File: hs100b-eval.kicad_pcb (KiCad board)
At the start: 2 copper layers, 60 x 50 mm, 42 parts, among them IC1 HS-100B, J1 SPKR, J2 MIC, J3 RADIO_DATA, SW1 MUTE_REC, SW2 MUTE_PLAY, SW3 VOL_DN, SW4 VOL_UP

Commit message: Add more test points
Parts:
- added TP1: GND, TestPoint:TestPoint_Pad_D2.0mm, F.Cu at (148.0, 72.0)
- added TP2: 5V, TestPoint:TestPoint_Pad_D1.0mm, F.Cu at (174.0, 74.0)
- TP3: renamed from TP1; value Test_3V3 -> 3V3
- moved TP3 38.0 mm to (148.5, 80.0)
- moved J1 2.50 mm to (138.0, 111.0)
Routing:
- net +3V3: track 72.6 -> 43.3 mm
- net /AUDIO_R: track 37.9 -> 22.4 mm, vias 2 -> 0
- net VBUS: track 37.8 -> 41.4 mm
- net /AUDIO_L: track 30.2 -> 26.8 mm
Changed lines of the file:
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@@
-(kicad_pcb (version 20171130) (host pcbnew 5.1.9)
+(kicad_pcb (version 20171130) (host pcbnew "(5.1.9-0-10_14)")
   (general
     (thickness 1.6)
     (drawings 8)
-    (tracks 333)
+    (tracks 323)
     (zones 0)
-    (modules 42)
+    (modules 44)
     (nets 37)
   )
@@
     (add_net /USB-)
   )
+  (module TestPoint:TestPoint_Pad_D1.0mm (layer F.Cu)
+    (at 174 74)
+    (descr "SMD pad as test Point, diameter 1.0mm")
+    (tags "test point SMD pad")
+    (attr virtual)
+    (fp_text reference TP2 (at 0 -1.448) (layer F.Fab)
+      (effects (font (size 1 1) (thickness 0.15)))
+    )
+    (fp_text value 5V (at 0 -1.5) (layer F.SilkS)
+      (effects (font (size 1 1) (thickness 0.15)))
+    )
+    (fp_circle (center 0 0) (end 0 0.7) (layer F.SilkS) (width 0.12))
+    (fp_circle (center 0 0) (end 1 0) (layer F.CrtYd) (width 0.05))
+    (fp_text user %R (at 0 -1.45) (layer F.Fab)
+      (effects (font (size 1 1) (thickness 0.15)))
+    )
+    (pad 1 smd circle (at 0 0) (size 1 1) (layers F.Cu F.Mask)
+      (net 4 VBUS))
+  )
+  (module TestPoint:TestPoint_Pad_D2.0mm (layer F.Cu)
+    (at 148 72)
+    (descr "SMD pad as test Point, diameter 2.0mm")
+    (tags "test point SMD pad")
+    (attr virtual)
+    (fp_text reference TP1 (at 0 -1.998) (layer F.Fab)
+      (effects (font (size 1 1) (thickness 0.15)))
+    )
+    (fp_text value GND (at 0 2.05) (layer F.SilkS)
+      (effects (font (size 1 1) (thickness 0.15)))
+    )
+    (fp_circle (center 0 0) (end 0 1.2) (layer F.SilkS) (width 0.12))
+    (fp_circle (center 0 0) (end 1.5 0) (layer F.CrtYd) (width 0.05))
+    (fp_text user %R (at 0 -2) (layer F.Fab)
+      (effects (font (size 1 1) (thickness 0.15)))
+    )
+    (pad 1 smd circle (at 0 0) (size 2 2) (layers F.Cu F.Mask)
+      (net 3 GND))
+  )
   (module Connector_Audio:Jack_3.5mm_CUI_SJ-3524-SMT_Horizontal (layer F.Cu)
-    (at 135.5 111 180)
+    (at 138 111 180)
     (descr "3.5 mm, Stereo, Right Angle, Surface Mount (SMT), Audio Jack Connector (https://www.cui.com/product/resource/sj-352x-smt-series.pdf)")
     (tags "3.5mm audio cui horizontal jack stereo")
@@
   )
   (module TestPoint:TestPoint_Pad_D1.0mm (layer F.Cu)
-    (at 142.5 117.5)
+    (at 148.5 80)
     (descr "SMD pad as test Point, diameter 1.0mm")
     (tags "test point SMD pad")
     (attr virtual)
-    (fp_text reference TP1 (at 0 -1.448) (layer F.SilkS)
-      (effects (font (size 1 1) (thickness 0.15)))
-    )
-    (fp_text value Test_3V3 (at 0 1.55) (layer F.SilkS)
+    (fp_text reference TP3 (at 0 -1.448) (layer F.Fab)
+      (effects (font (size 1 1) (thickness 0.15)))
+    )
+    (fp_text value 3V3 (at 0 -1.5) (layer F.SilkS)
       (effects (font (size 1 1) (thickness 0.15)))
     )
@@
   (segment (start 170.8 78.8) (end 175 83) (width 0.35) (layer F.Cu) (net 4))
   (segment (start 170.8 75) (end 170.8 78.8) (width 0.35) (layer F.Cu) (net 4))
+  (segment (start 171.8 74) (end 170.8 75) (width 0.35) (layer F.Cu) (net 4))
+  (segment (start 174 74) (end 171.8 74) (width 0.35) (layer F.Cu) (net 4))
   (segment (start 134 74) (end 144 74) (width 0.25) (layer F.Cu) (net 5))
   (segment (start 151.728202 84.5) (end 147.680998 84.5) (width 0.25) (layer F.Cu) (net 5))
@@
   (segment (start 142.824999 79.644001) (end 142.824999 75.175001) (width 0.25) (layer F.Cu) (net 5))
   (segment (start 157.23751 93.490692) (end 157.23751 90.009308) (width 0.25) (layer F.Cu) (net 5))
-  (segment (start 147.680998 84.5) (end 142.824999 79.644001) (width 0.25) (layer F.Cu) (net 5))
   (segment (start 156.978202 93.75) (end 157.23751 93.490692) (width 0.25) (layer F.Cu) (net 5))
   (segment (start 156.175 93.75) (end 156.978202 93.75) (width 0.25) (layer F.Cu) (net 5))
-  (segment (start 142.5 108.328606) (end 142.5 117.5) (width 0.25) (layer F.Cu) (net 5))
-  (segment (start 147.553607 103.274999) (end 142.5 108.328606) (width 0.25) (layer F.Cu) (net 5))
-  (segment (start 151.739999 103.274999) (end 147.553607 103.274999) (width 0.25) (layer F.Cu) (net 5))
-  (segment (start 153.600001 94.149999) (end 153.600001 101.414997) (width 0.25) (layer F.Cu) (net 5))
-  (segment (start 154 93.75) (end 153.600001 94.149999) (width 0.25) (layer F.Cu) (net 5))
-  (segment (start 153.600001 101.414997) (end 151.739999 103.274999) (width 0.25) (layer F.Cu) (net 5))
-  (segment (start 156.175 93.75) (end 154 93.75) (width 0.25) (layer F.Cu) (net 5))
+  (segment (start 148.5 80) (end 145.965499 82.534501) (width 0.25) (layer F.Cu) (net 5))
+  (segment (start 145.965499 82.534501) (end 145.965499 82.784501) (width 0.25) (layer F.Cu) (net 5))
+  (segment (start 145.965499 82.784501) (end 142.824999 79.644001) (width 0.25) (layer F.Cu) (net 5))
+  (segment (start 147.680998 84.5) (end 145.965499 82.784501) (width 0.25) (layer F.Cu) (net 5))
   (segment (start 139 90.4) (end 136.25 90.4) (width 0.25) (layer F.Cu) (net 6))
   (segment (start 139.68749 91.08749) (end 139 90.4) (width 0.25) (layer F.Cu) (net 6))
@@
   (segment (start 170.72501 104.65001) (end 174.82499 104.65001) (width 0.25) (layer F.Cu) (net 13))
   (segment (start 169.075 103) (end 170.72501 104.65001) (width 0.25) (layer F.Cu) (net 13))
-  (segment (start 132.075001 112.324999) (end 135.460003 112.324999) (width 0.25) (layer F.Cu) (net 14))
-  (segment (start 135.460003 112.324999) (end 145.9 101.885002) (width 0.25) (layer F.Cu) (net 14))
-  (segment (start 131.8 112.6) (end 132.075001 112.324999) (width 0.25) (layer F.Cu) (net 14))
-  (segment (start 145.9 101.885002) (end 145.9 95) (width 0.25) (layer F.Cu) (net 14))
-  (segment (start 131.8 113.1) (end 132.075001 112.824999) (width 0.25) (layer F.Cu) (net 14))
   (segment (start 145.9 94) (end 143.5 91.6) (width 0.25) (layer F.Cu) (net 14))
   (segment (start 145.9 95) (end 145.9 94) (width 0.25) (layer F.Cu) (net 14))
+  (segment (start 134.3 108.460998) (end 134.3 112.6) (width 0.25) (layer F.Cu) (net 14))
+  (segment (start 145.9 96.860998) (end 134.3 108.460998) (width 0.25) (layer F.Cu) (net 14))
+  (segment (start 145.9 95) (end 145.9 96.860998) (width 0.25) (layer F.Cu) (net 14))
   (segment (start 152.1 92.4) (end 152.25 92.25) (width 0.25) (layer F.Cu) (net 15))
   (via (at 152.25 92.25) (size 0.8) (drill 0.4) (layers F.Cu B.Cu) (net 15))
@@
   (segment (start 154.524999 88.524999) (end 158.25 92.25) (width 0.25) (layer B.Cu) (net 15))
   (segment (start 163 92.25) (end 164.5 92.25) (width 0.25) (layer F.Cu) (net 15))
-  (via (at 140 102) (size 0.8) (drill 0.4) (layers F.Cu B.Cu) (net 16))
-  (segment (start 139.2 102.8) (end 140 102) (width 0.25) (layer F.Cu) (net 16))
-  (segment (start 139.2 105.7) (end 139.2 102.8) (width 0.25) (layer F.Cu) (net 16))
-  (segment (start 150.725001 91.725001) (end 148 89) (width 0.25) (layer B.Cu) (net 16))
-  (segment (start 150.725001 104.348001) (end 150.725001 91.725001) (width 0.25) (layer B.Cu) (net 16))
-  (segment (start 150.348001 104.725001) (end 150.725001 104.348001) (width 0.25) (layer B.Cu) (net 16))
-  (via (at 148 89) (size 0.8) (drill 0.4) (layers F.Cu B.Cu) (net 16))
-  (segment (start 142.725001 104.725001) (end 150.348001 104.725001) (width 0.25) (layer B.Cu) (net 16))
-  (segment (start 140 102) (end 142.725001 104.725001) (width 0.25) (layer B.Cu) (net 16))
-  (segment (start 148 89) (end 145.9 89) (width 0.25) (layer F.Cu) (net 16))
   (segment (start 145.4625 89) (end 143.4625 87) (width 0.25) (layer F.Cu) (net 16))
   (segment (start 145.9 89) (end 145.4625 89) (width 0.25) (layer F.Cu) (net 16))
+  (segment (start 147.400001 96.485001) (end 147.400001 90.500001) (width 0.25) (layer F.Cu) (net 16))
+  (segment (start 147.400001 90.500001) (end 145.9 89) (width 0.25) (layer F.Cu) (net 16))
+  (segment (start 141.7 102.185002) (end 147.400001 96.485001) (width 0.25) (layer F.Cu) (net 16))
+  (segment (start 141.7 105.2) (end 141.7 102.185002) (width 0.25) (layer F.Cu) (net 16))
   (via (at 154 89.25) (size 0.8) (drill 0.4) (layers F.Cu B.Cu) (net 17))
   (segment (start 153.75 89) (end 154 89.25) (width 0.25) (layer F.Cu) (net 17))

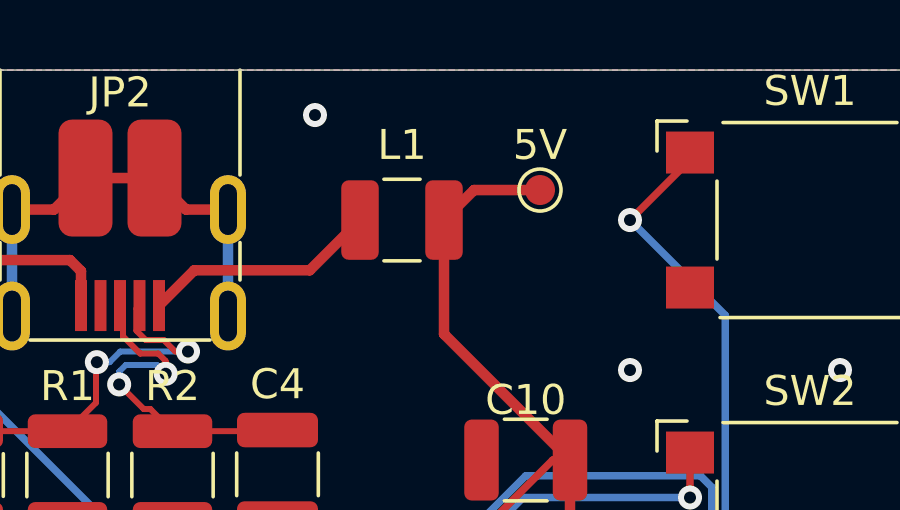
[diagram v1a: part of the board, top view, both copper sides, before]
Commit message: Move 5V test point to directly off USB
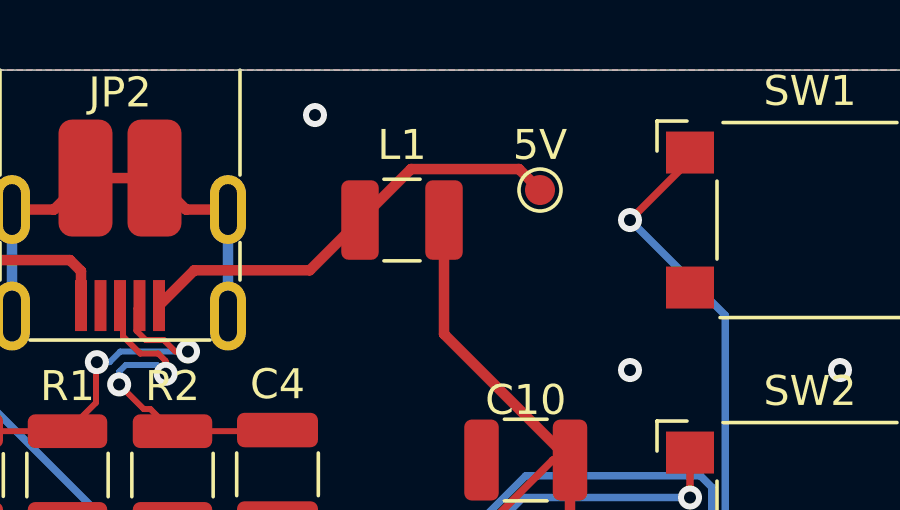
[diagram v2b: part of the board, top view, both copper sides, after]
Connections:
- TP2 pad 1: VBUS -> Net-(JP2-Pad1)
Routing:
- net Net-(JP2-Pad1): track 7.88 -> 14.9 mm
- net VBUS: track 41.4 -> 37.8 mm

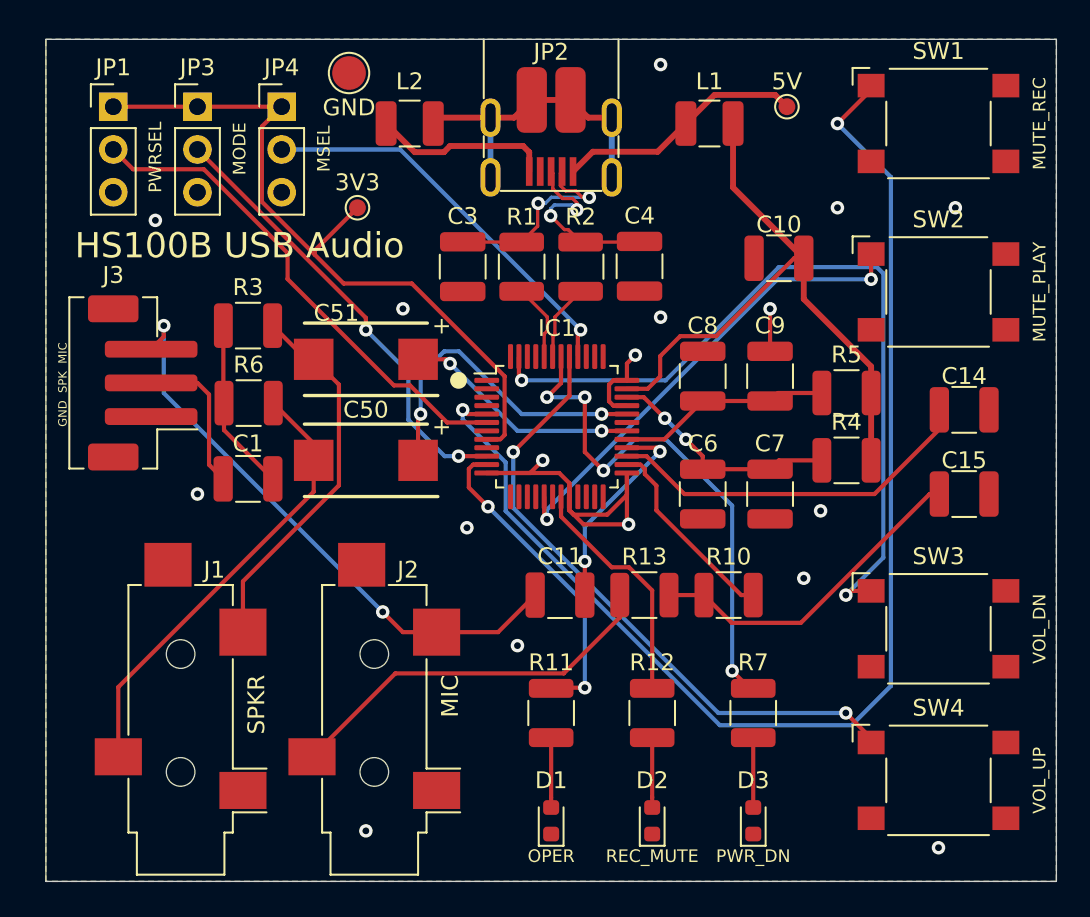
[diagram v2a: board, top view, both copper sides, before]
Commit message: Incorporate learnings from first physical prototype
* Button footprint pad numberings are wrong for symbol, so they were always pressed
* Turn J3 for solderability
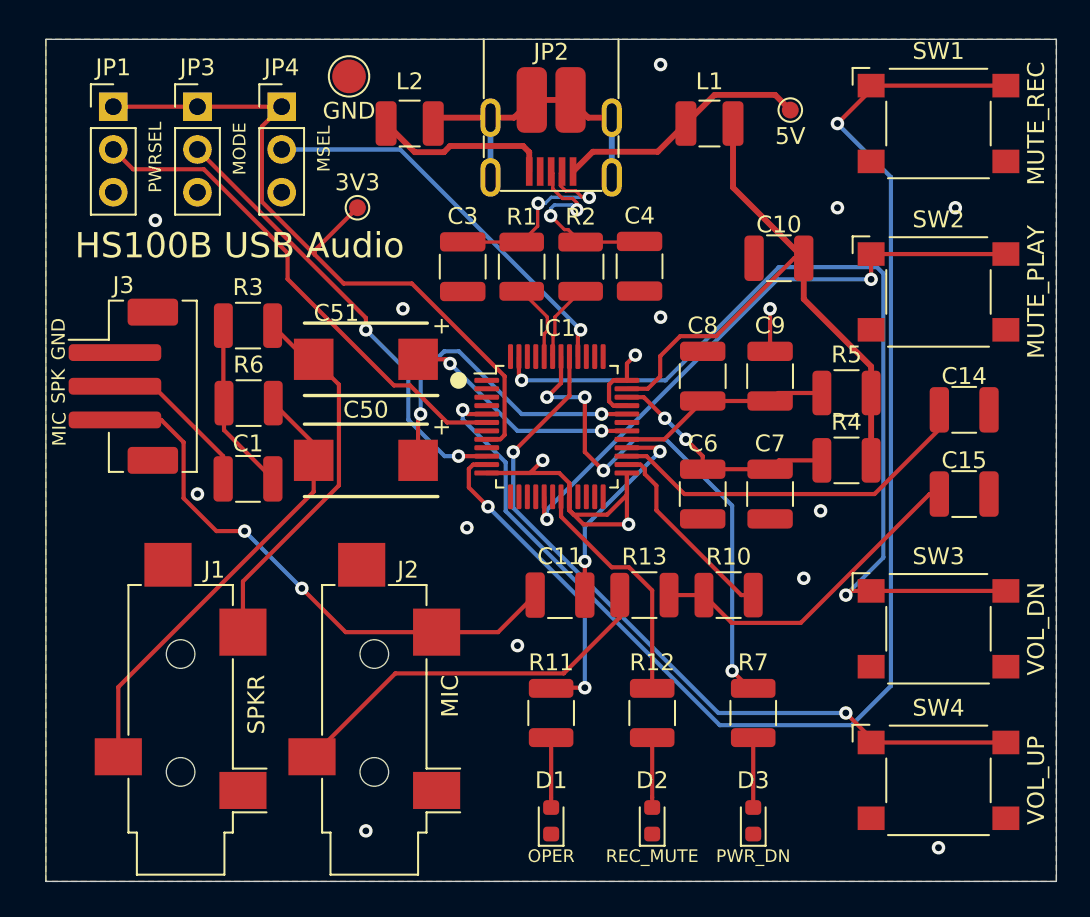
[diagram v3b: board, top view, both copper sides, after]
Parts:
- SW1, SW2, SW3, SW4: footprint Button_Switch_SMD:SW_SPST_Omron_B3FS-100xP -> Omron:SW_SPST_Omron_B3FS-100xP
- moved J3 1.17 mm to (134.6, 90.6), turned to 270 degrees
- moved TP2 0.28 mm to (174.2, 74.2)
- moved TP1 0.20 mm to (148.0, 72.2)
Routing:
- net /VOLUP: track 37.5 -> 45.5 mm
- net /VOLDN: track 47.5 -> 55.5 mm
- net /MUTER: track 75.5 -> 83.5 mm
- net /MUTEP: track 28.4 -> 36.4 mm
- net /MIC_IN: track 34.6 -> 33.0 mm
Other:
- board text added: "HS100B Audio Evaluation Board v2 C. Keller 2021-04-18 https://github.com/k0swe/hs100b-eval"
- board text removed: "GND SPK MIC"
- board text removed: "HS100B Audio Evaluation Board v2 C. Keller 2021-04-14"

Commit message: Fix R and L on J1
Resolves #1
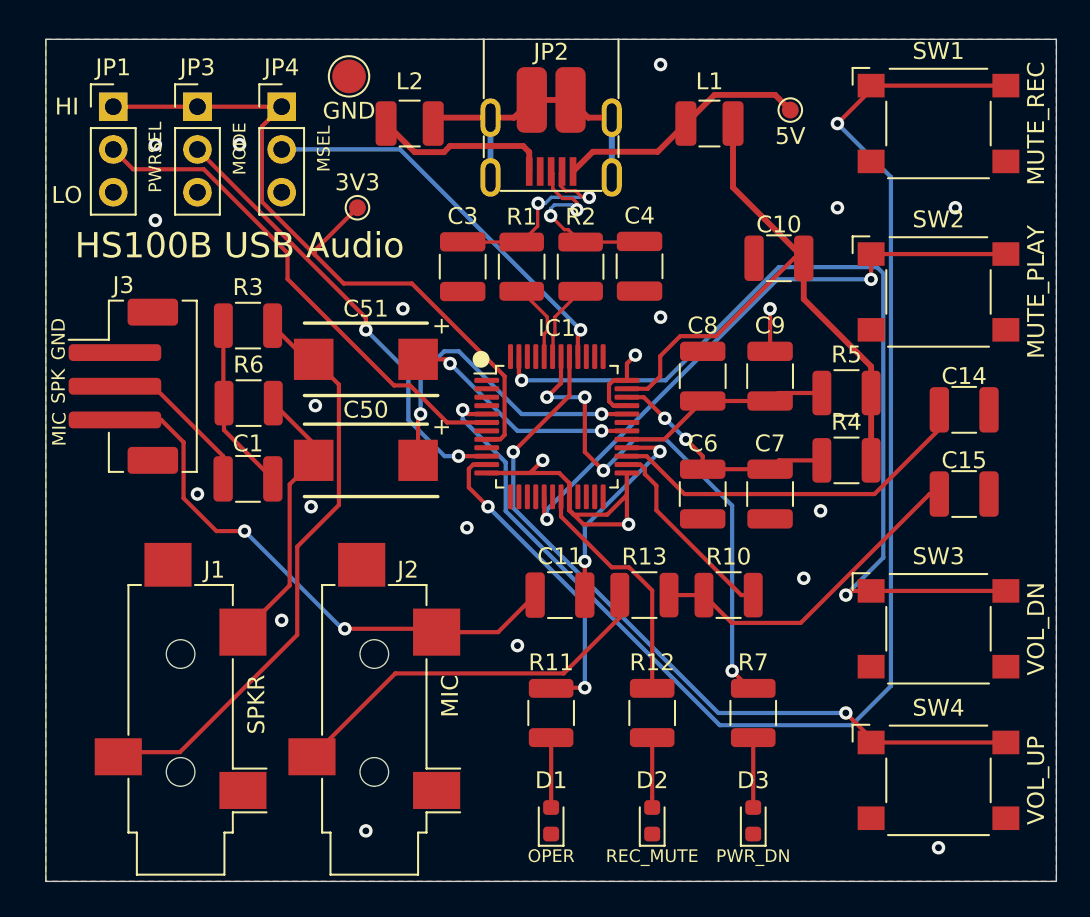
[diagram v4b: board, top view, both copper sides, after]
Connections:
- J1 pad R: /AUDIO_L -> /AUDIO_R
- J1 pad T: /AUDIO_R -> /AUDIO_L
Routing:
- net /AUDIO_R: track 22.4 -> 34.9 mm
- net /AUDIO_L: track 26.8 -> 16.3 mm
- net GND: vias 17 -> 22
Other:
- board text added: "HI"
- board text added: "HS100B Audio Evaluation Board v3 C. Keller 2021-04-21 https://github.com/k0swe/hs100b-eval"
- board text added: "LO"
- board text removed: "HS100B Audio Evaluation Board v2 C. Keller 2021-04-18 https://github.com/k0swe/hs100b-eval"

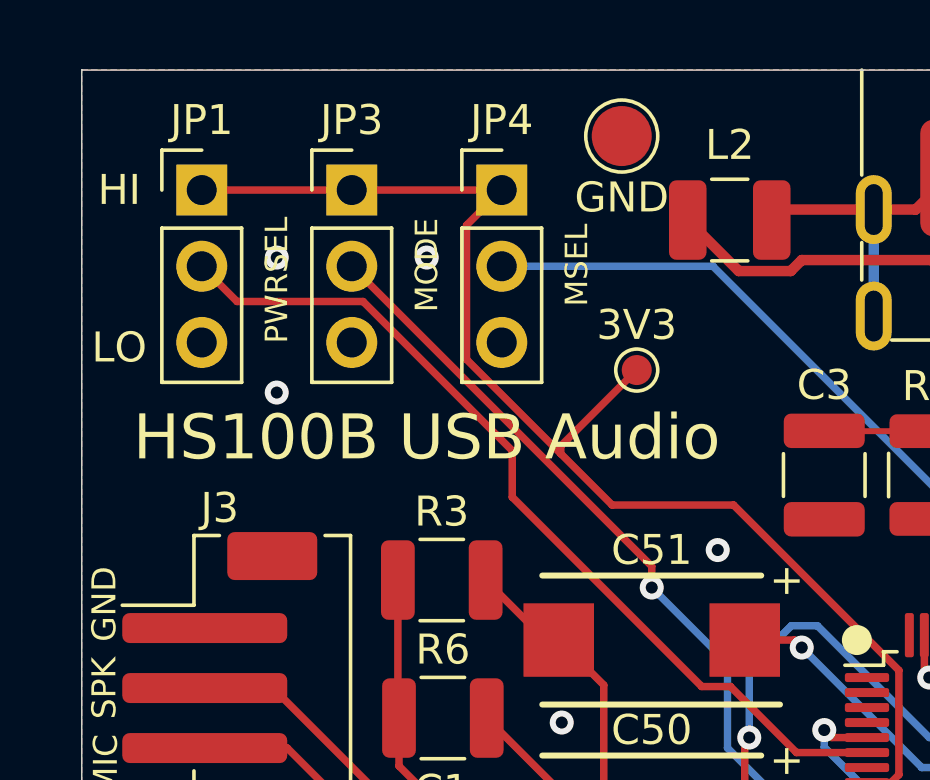
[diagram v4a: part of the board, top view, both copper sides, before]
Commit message: Move to DIP switches for config
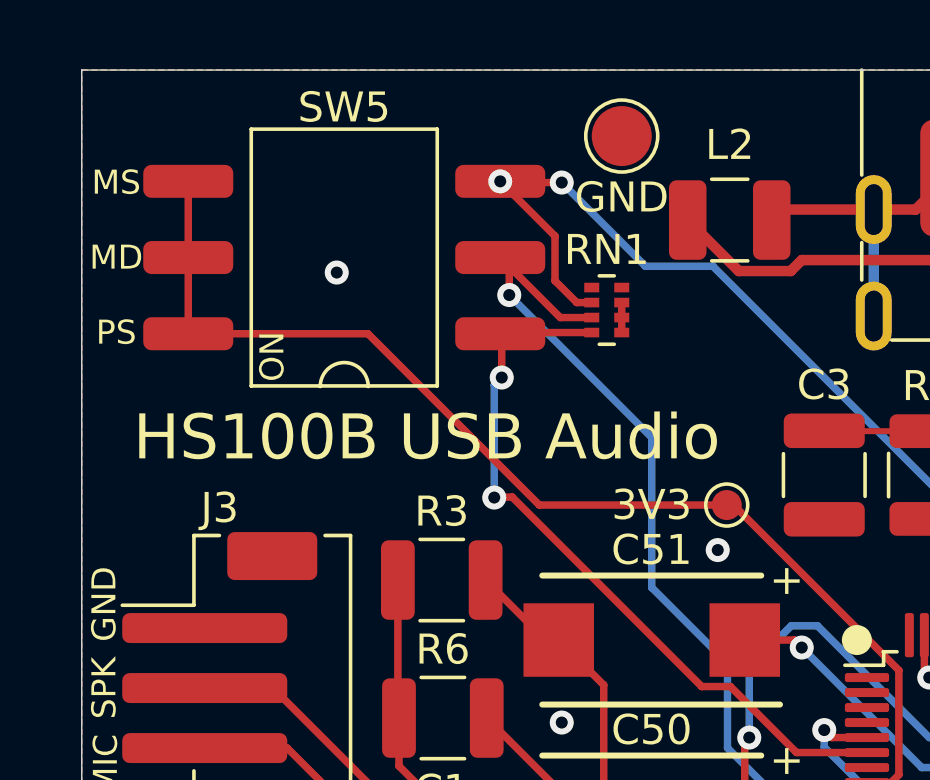
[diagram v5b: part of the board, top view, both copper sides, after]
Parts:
- removed JP1: PWRSEL, Connector_PinHeader_2.54mm:PinHeader_1x03_P2.54mm_Vertical
- removed JP3: MODE, Connector_PinHeader_2.54mm:PinHeader_1x03_P2.54mm_Vertical
- removed JP4: MSEL, Connector_PinHeader_2.54mm:PinHeader_1x03_P2.54mm_Vertical
- added RN1: 10KΩ, Resistor_SMD:R_Array_Concave_4x0402, F.Cu at (147.5, 78.0)
- added SW5: SW_DIP_x03, Diptronics:DMR, F.Cu at (138.8, 76.2)
- moved TP3 5.41 mm to (151.5, 84.5)
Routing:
- net /MSEL: track 23.8 -> 30.7 mm, vias 1 -> 3
- net +3V3: track 43.3 -> 38.1 mm
- net /PWRSEL: track 29.8 -> 24.6 mm, vias 0 -> 2
- net /MODE: track 26.8 -> 28.9 mm
- net GND: track 42.2 -> 43.2 mm, vias 22 -> 20
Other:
- board text removed: "HI"
- board text removed: "LO"

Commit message: Renumber components
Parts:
- removed D3: PWR_DN, LED_SMD:LED_0603_1608Metric
- removed the R7 at (172.0, 110.0)
- added R1: 0Ω, Resistor_SMD:R_1210_3225Metric, F.Cu at (174.0, 84.5)
- L1, L2: value L -> Ferrite_Bead
- moved C12 18.1 mm to (172.0, 110.0), turned to 90 degrees
- moved C9 10.3 mm to (177.5, 99.5)
- moved C1 2.79 mm to (174.0, 80.2)
- moved TP3 2.75 mm to (148.8, 84.5)
- renumbered C10 to C1, C50 to C10, C51 to C11, C15 to C12, C11 to C13, C1 to C21, C9 to C3, C8 to C4, C7 to C5, C4 to C7, C3 to C8, C14 to C9, JP2 to J1, J1 to J2, J3 to J20, J2 to J3, R5 to R2, R3 to R21, R6 to R22, R4 to R3, R2 to R4, R1 to R5, R10 to R6, R13 to R7, R11 to R8, R12 to R9
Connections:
- IC1 pad 35: VBUS -> Net-(IC1-Pad35)
- IC1 pad 42: /PDSW -> (no net)
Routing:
- net /PDSW: track 31.4 -> 0.00 mm, vias 4 -> 0
- net VBUS: track 37.8 -> 23.4 mm
- net Net-(IC1-Pad35): track 0.00 -> 11.1 mm
- net Net-(C12-Pad2): track 19.9 -> 8.81 mm
- net Net-(C9-Pad2): track 22.2 -> 14.3 mm
- net Net-(D3-Pad2): track 4.15 -> 0.00 mm
- net GND: track 43.2 -> 40.7 mm, vias 20 -> 18
